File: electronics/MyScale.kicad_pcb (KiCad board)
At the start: 4 copper layers, 83.5 x 64.7 mm, 97 parts, among them J1 Conn_01x03, J10 Conn_02x03_Odd_Even, J2 Conn_01x03, J3 Conn_01x03, J4 Conn_01x03, J5 Conn_01x02_MountingPin, J6 12402012E212A, J7 SIM_Card, J9 Conn_Coaxial_Small, Q1 Q_NMOS_GSD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

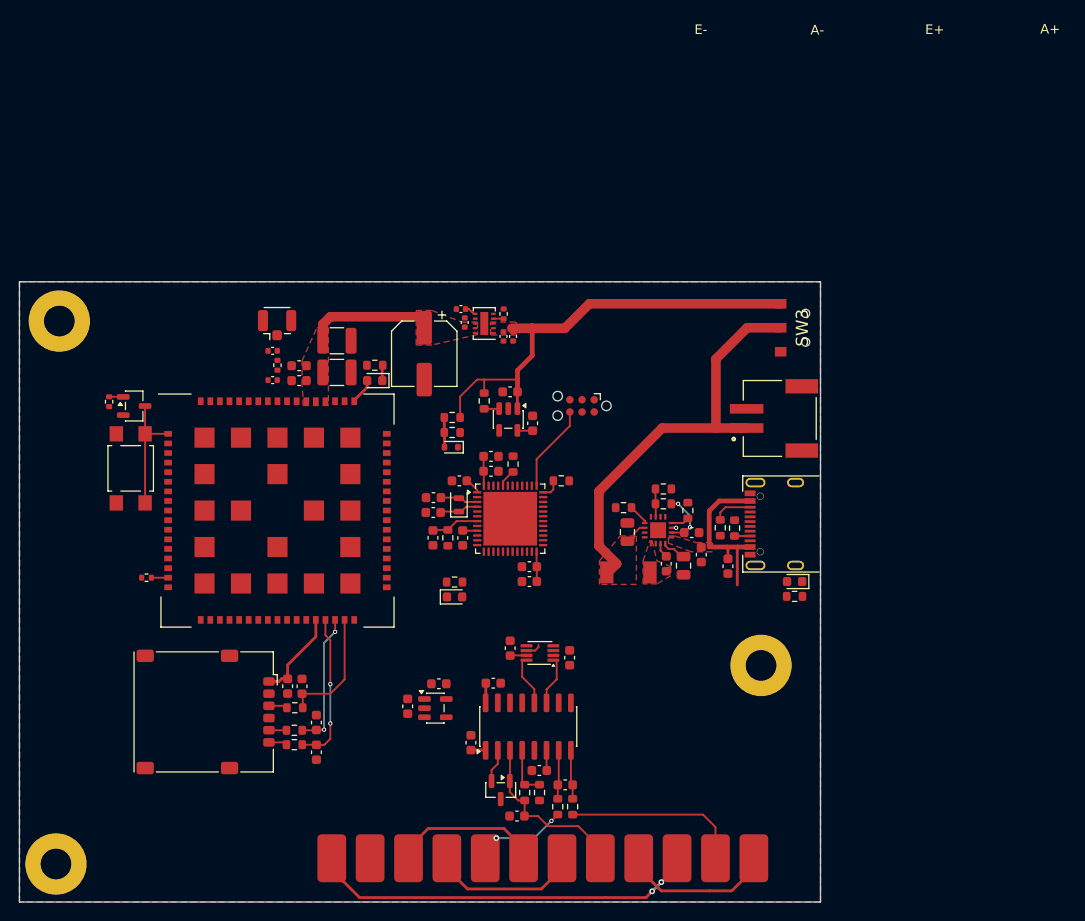
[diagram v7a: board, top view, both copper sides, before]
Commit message: electronics: replace A7670 footprint
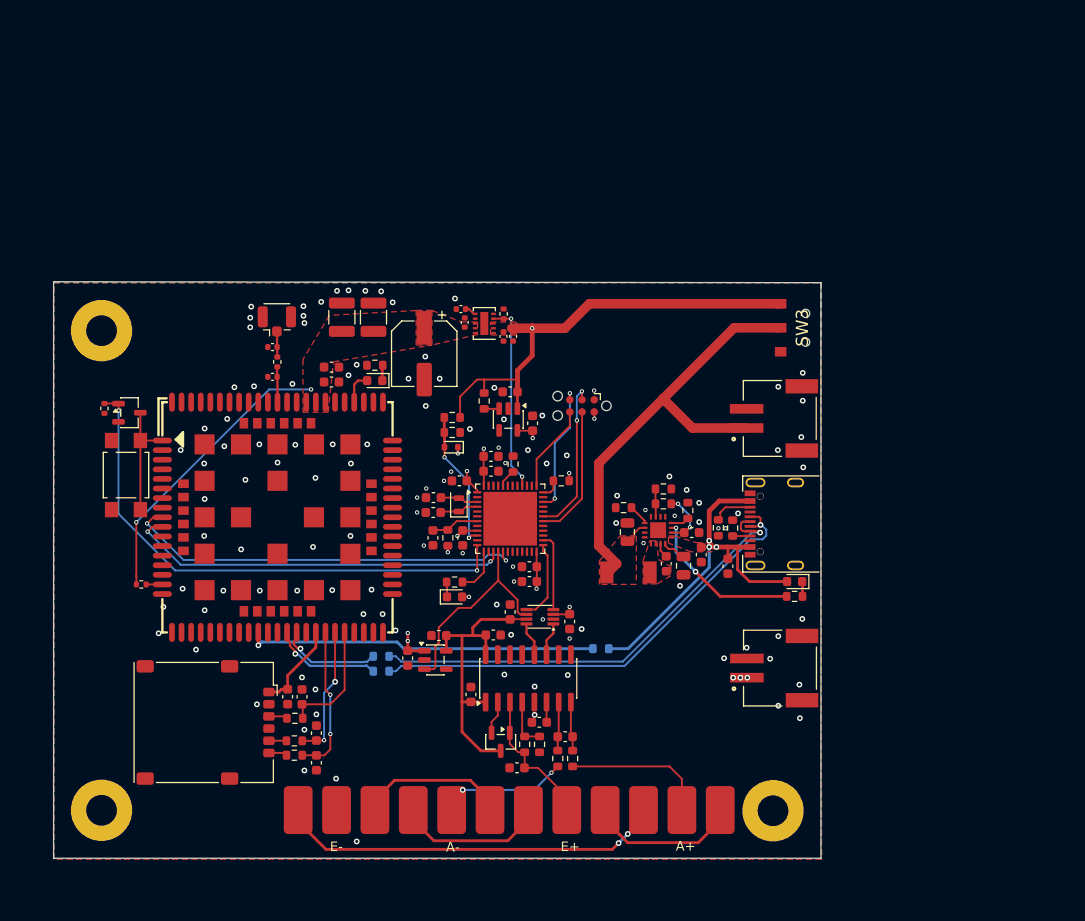
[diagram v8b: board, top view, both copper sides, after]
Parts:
- added J8: Conn_01x02_MountingPin, MyScale:JST_S2B-PH-SM4-TB(LF)(SN), F.Cu at (140.7, 155.2)
- added R27: 27R, Resistor_SMD:R_0603_1608Metric, B.Cu at (99.2, 153.9)
- added R28: 27R, Resistor_SMD:R_0603_1608Metric, B.Cu at (99.2, 155.5)
- added R29: 0R, Resistor_SMD:R_0603_1608Metric, B.Cu at (122.0, 153.2)
- U4: footprint MyScale:A7670 -> MyScale:A7670_STAMP
- moved H1 15.2 mm to (140.0, 170.1)
- moved H3 7.34 mm to (70.0, 170.0)
- moved C25 6.90 mm to (98.3, 118.6), turned to 90 degrees
- moved J1 6.12 mm to (90.5, 170.0)
- moved J2 6.12 mm to (102.5, 170.0)
- moved J3 6.12 mm to (114.5, 170.0)
- moved J4 6.12 mm to (126.5, 170.0)
- moved C12 5.03 mm to (115.6, 160.8)
- moved C14 5.03 mm to (110.8, 151.7)
- moved C15 5.03 mm to (113.3, 165.6)
- moved C16 5.03 mm to (118.3, 162.3)
- moved C36 5.03 mm to (101.9, 154.1)
- moved C37 5.03 mm to (105.2, 151.8)
- moved R18 5.03 mm to (114.1, 163.1)
- moved R19 5.03 mm to (115.7, 163.1)
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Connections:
- J10 pad 2: VCC -> +1V8
- J6 pad A6: /USBD+ -> /USBCD+
- J6 pad A7: /USBD- -> /USBCD-
- J6 pad B6: /USBD+ -> /USBCD+
- J6 pad B7: /USBD- -> /USBCD-
- U4 pad 24: VBUS -> Net-(U4-VBUS)
- U4 pad 26: Net-(U4-NC-Pad26) -> unconnected-(U4-NC-Pad26)
- U4 pad 35: Net-(U4-NC-Pad26) -> unconnected-(U4-NC-Pad35)
- U4 pad 36: Net-(U4-NC-Pad26) -> unconnected-(U4-NC-Pad36)
- U4 pad 44: Net-(U4-NC-Pad26) -> unconnected-(U4-NC-Pad44)
- U4 pad 47: Net-(U4-NC-Pad26) -> unconnected-(U4-NC-Pad47)
- U4 pad 51: Net-(U4-NC-Pad26) -> unconnected-(U4-NC-Pad51)
- U4 pad 53: Net-(U4-NC-Pad26) -> unconnected-(U4-NC-Pad53)
- U5 pad 12: unconnected-(U5-PA2-Pad12) -> /RadioPwrKey
- U5 pad 13: unconnected-(U5-PA3-Pad13) -> /Led
- U5 pad 15: unconnected-(U5-PA5-Pad15) -> /RadioUartTx
- U5 pad 16: unconnected-(U5-PA6-Pad16) -> /CellsEnable
- U5 pad 17: unconnected-(U5-PA7-Pad17) -> /RadioUartRx
- U5 pad 25: unconnected-(U5-PB12-Pad25) -> /Dout
- U5 pad 26: unconnected-(U5-PB13-Pad26) -> /Sck
- U5 pad 30: unconnected-(U5-PA9-Pad30) -> /UartTx
- U5 pad 31: unconnected-(U5-PA10-Pad31) -> /UartRx
- U5 pad 40: unconnected-(U5-PB4-Pad40) -> /RadioEnable
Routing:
- net /RadioPwrKey: track 1.48 -> 55.4 mm, vias 0 -> 2
- net /USBCD+: track 0.00 -> 49.6 mm, vias 0 -> 1
- net /USBCD-: track 0.00 -> 48.3 mm, vias 0 -> 1
- net /RadioUartRx: track 0.00 -> 42.3 mm, vias 0 -> 2
- net VBAT: track 48.4 -> 90.0 mm, vias 0 -> 3
- net /RadioUartTx: track 0.00 -> 40.2 mm, vias 0 -> 2
- net VBUS: track 17.9 -> 56.1 mm, vias 0 -> 6
- net Net-(U4-VBUS): track 0.00 -> 36.7 mm, vias 0 -> 1
- net +3V3: track 5.31 -> 32.0 mm
- net /CellsEnable: track 1.64 -> 21.9 mm
- net /RadioEnable: track 1.07 -> 19.8 mm, vias 0 -> 2
- net /Radio/VbatModule: track 12.6 -> 30.4 mm, vias 0 -> 2
- net /UartRx: track 0.00 -> 16.4 mm, vias 0 -> 2
- net Net-(U8-STAT): track 0.48 -> 16.5 mm, vias 1 -> 2
- net /UartTx: track 0.00 -> 14.1 mm
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- added copper zone on In2.Cu, net +1V8
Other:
- board size 83.5 x 64.7 mm -> 80 x 60.1 mm
